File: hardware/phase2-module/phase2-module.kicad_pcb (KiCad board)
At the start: 4 copper layers, 130 x 90 mm, 180 parts, among them J1 XT60PW-M SLOT PWR, J2 SWD, J3 UART, J4 XT60PW-M OUTPUT, J5 SLOT SIGNALS, J6 FAN, Q1 CSD18540Q5B, Q10 CSD18540Q5B, Q11 CSD18540Q5B, Q12 CSD18540Q5B, Q13 CSD18540Q5B, Q14 CSD19536KTT, Q2 CSD18540Q5B, Q3 CSD18540Q5B, Q4 CSD18540Q5B, Q5 2N7002, Q6 2N7002, Q7 2N7002, Q8 2N7002, Q9 2N7002, U1 DAC80502DRXT, U10 STM32G431CBT6, U11 TCAN1042HGV, U12 LM5069MM-2, U13 TS5A3166, U2 OPA2333, U3 LM5143RHAR, U4 INA240A3, U5 INA228, U6 LTC7004, U7 TLV7011DCK, U8 LMR36015AQRNXRQ1, U9 NCP1117-3.3, Y1 8MHz

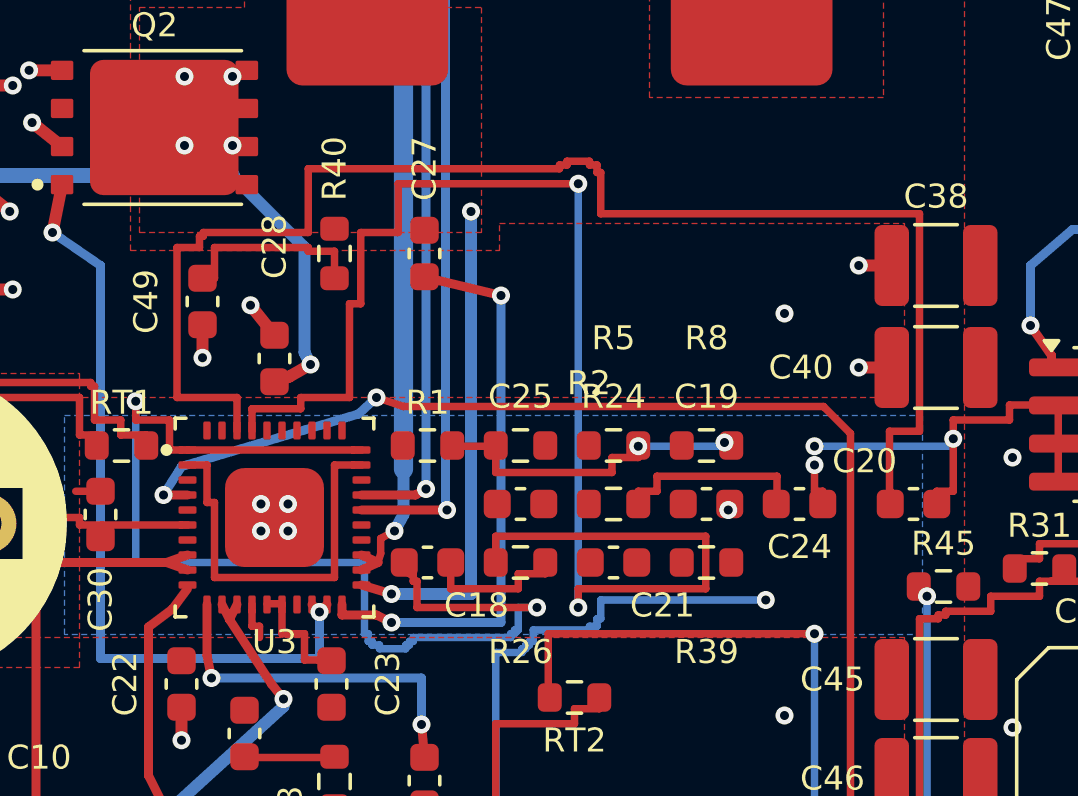
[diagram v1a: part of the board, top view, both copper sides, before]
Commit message: Phase-2 batch 1/6 (u3 pocket): finish_routes.py + PS_RT wall teardown
finish_routes.py: declarative waypoint router in the route_board tradition
with an exact analytic clearance validator (point-to-track/via/pad-rect
distances, per-pad local clearances, DEL modeling during --check). Zero
rasterization: the bitmap approach false-blocked exactly-legal 0.2mm
geometry all over the QFN field.

Board changes (83 -> 84 unconnected, 0 new copper DRC):
- PS_RT: DELETED the autorouter's pocket "walls" (y35.62/y37.38/x90.38/
  x86.12 tail, 8 items) - its 60mm round-trip approach sealed every
  east-west route in the AGND pocket. Net intentionally split (+1 item);
  A* fallback completes the tail.
- PS_COMP: deleted pin2's dangling y37.0 wander (2 items) - opens the
  south corridor; pin2/pin29/R24.1/C25.1 all go to A*.
- PS_DITH: routed R39.1 -> y35.55 lane -> via pair across the x95.2
  PH_CS_B vertical on B.Cu -> C20.1 (-1 item).
- PS_EN: pin40 west escape via (73.15,31.65).

A* fallback list (sealed-pin escapes where hand routing is geometrically
impossible at 0.2mm clearance - every lane owned by RT staircase, C-pad,
DITH vertical, PH_CS_B/G_HS_A/BST_A columns, FB spine, PS_SS escape):
PS_VDDA, PS_RES, PS_FPWM, PS_VIN, PS_PGOOD, VOUT_INT pin5, FB pin28,
PS_EN pin31, PS_VCC, PS_COMP cluster, PS_RT tail.

Hard-won geometry facts now encoded in the tool comments: U3's top row
is sealed by the RT staircase + (76.0,30.5) C-pad; the right column by
0.5mm pitch at 0.25 pad gap; the pocket east-west by FB spine y33.5 +
COMP_Z y33.62; B.Cu crossings by SW1 x82.55 / G_HS_A x80.3 / BST_A
x83.55 columns spanning y7-38.
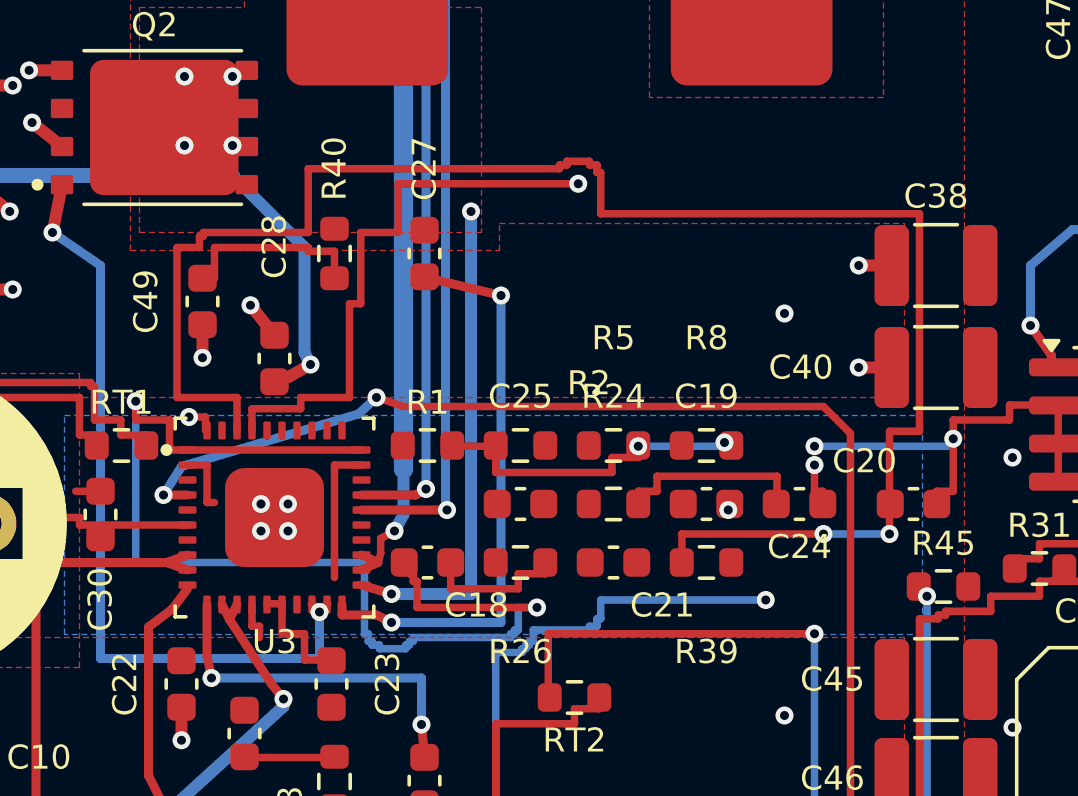
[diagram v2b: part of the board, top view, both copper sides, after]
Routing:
- net PS_RT: track 47.8 -> 19.1 mm, vias 2 -> 1
- net PS_DITH: track 48.2 -> 56.6 mm, vias 0 -> 2
- net PS_COMP: track 13.3 -> 6.78 mm
- net PS_EN: track 8.66 -> 9.66 mm, vias 0 -> 1

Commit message: Phase-2 A* fallback pass: 84 -> 82 unconnected; net filter for autoroute
autoroute.py: argv net filter (route ONLY named nets - fallback mode for
finish_routes.py's sealed-pin list; running unfiltered on the current
board would duplicate copper).

Fallback pass on 9 pocket nets: 2 routed (PS_EN pin31 to its trunk; one
more), 10 'no path' fails - all from U3's sealed pins. The grid router
confirms the analytic finding: pins 24/25/28/32/33/34/36 have no legal
escape at any clearance the board allows; they were among the original
autoroute's fails too. Remaining strategy for them: junk-copper surgery
(the PS_RT-wall/pin2-wander class of DELs) or interactive push-and-shove.

4 transient danglers (2 tracks, 2 vias) from the partial routes - their
far ends connect in the haul batch. 0 copper clearance violations.
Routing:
- net PS_VDDA: track 0.00 -> 6.47 mm
- net PS_COMP: track 6.78 -> 11.6 mm
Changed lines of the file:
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@@
+	)
+	(segment
+		(start 103.375 55.375)
+		(end 103.375 54.5)
+		(width 0.25)
+		(layer "F.Cu")
+		(net "PS_COMP")
+	)
+	(segment
+		(start 105.875 55.375)
+		(end 103.375 55.375)
+		(width 0.25)
+		(layer "F.Cu")
+		(net "PS_COMP")
+	)
+	(segment
+		(start 105.875 54.875)
+		(end 105.875 55.375)
+		(width 0.25)
+		(layer "F.Cu")
+		(net "PS_COMP")
 	)
 	(segment
@@
 		(start 93.75 54.5)
 		(end 93.75 53.25)
+		(width 0.25)
+		(layer "F.Cu")
+		(net "PS_COMP")
+	)
+	(segment
+		(start 106.475 54.875)
+		(end 106.475 54.55)
+		(width 0.25)
+		(layer "F.Cu")
+		(net "PS_COMP")
+	)
+	(segment
+		(start 106.475 54.875)
+		(end 105.875 54.875)
 		(width 0.25)
 		(layer "F.Cu")
@@
 	)
 	(segment
+		(start 106.525 56.875)
+		(end 106.525 56.5)
+		(width 0.25)
+		(layer "F.Cu")
+		(net "PS_VDDA")
+	)
+	(segment
+		(start 107.25 56.875)
+		(end 107.25 57.375)
+		(width 0.25)
+		(layer "F.Cu")
+		(net "PS_VDDA")
+	)
+	(segment
+		(start 110.375 56.5)
+		(end 111.25 56.5)
+		(width 0.25)
+		(layer "F.Cu")
+		(net "PS_VDDA")
+	)
+	(segment
+		(start 106.525 56.875)
+		(end 107.25 56.875)
+		(width 0.25)
+		(layer "F.Cu")
+		(net "PS_VDDA")
+	)
+	(segment
+		(start 110.375 57.375)
+		(end 110.375 56.5)
+		(width 0.25)
+		(layer "F.Cu")
+		(net "PS_VDDA")
+	)
+	(segment
+		(start 107.25 57.375)
+		(end 110.375 57.375)
+		(width 0.25)
+		(layer "F.Cu")
+		(net "PS_VDDA")
+	)
+	(segment

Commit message: Phase-2 batch 2 start: A* open-field pass, 82 -> 81 unconnected
Autoroute filter pass over 29 open-field nets (U10 cluster + haul + aux):
most fails are NOT sealed pins - diag_grid shows free sources and exits
at every failing pad - but U10's escape CHANNELS need bundle planning:
the right/left rows (1.48mm-long pads, 0.5mm pitch) seal between-pad
gaps exactly like U3; escapes must turn OUTSIDE the pad-shadow strip
(x77.2/79.1 west/east, y73.0/83.0 north/south). finish_routes.py's u10
tables drafted wrong-direction escapes (west through the body) - rewrite
needed with per-side lanes before applying.

Kept the pass's 2 tracks + 1 via (one item resolved, 0 new violations;
the 2 danglers pre-existed).
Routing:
- net AGND: track 229.4 -> 229.8 mm, vias 89 -> 90
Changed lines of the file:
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@@
+	)
+	(segment
+		(start 108.125 56.125)
+		(end 108.075 56.125)
+		(width 0.25)
+		(layer "F.Cu")
+		(net "AGND")
 	)
 	(segment
@@
 	)
 	(segment
+		(start 108.075 56.125)
+		(end 108.075 56.5)
+		(width 0.25)
+		(layer "F.Cu")
+		(net "AGND")
+	)
+	(segment
 		(start 116.125 96.75)
 		(end 116.175 96.75)
@@
 		(net "AGND")
 	)
+	(via
+		(at 108.125 56.125)
+		(size 0.6)
+		(drill 0.3)
+		(layers "F.Cu" "B.Cu")
+		(net "AGND")
+	)
